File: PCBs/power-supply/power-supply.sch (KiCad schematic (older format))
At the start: 13 parts, among them U3 TL783

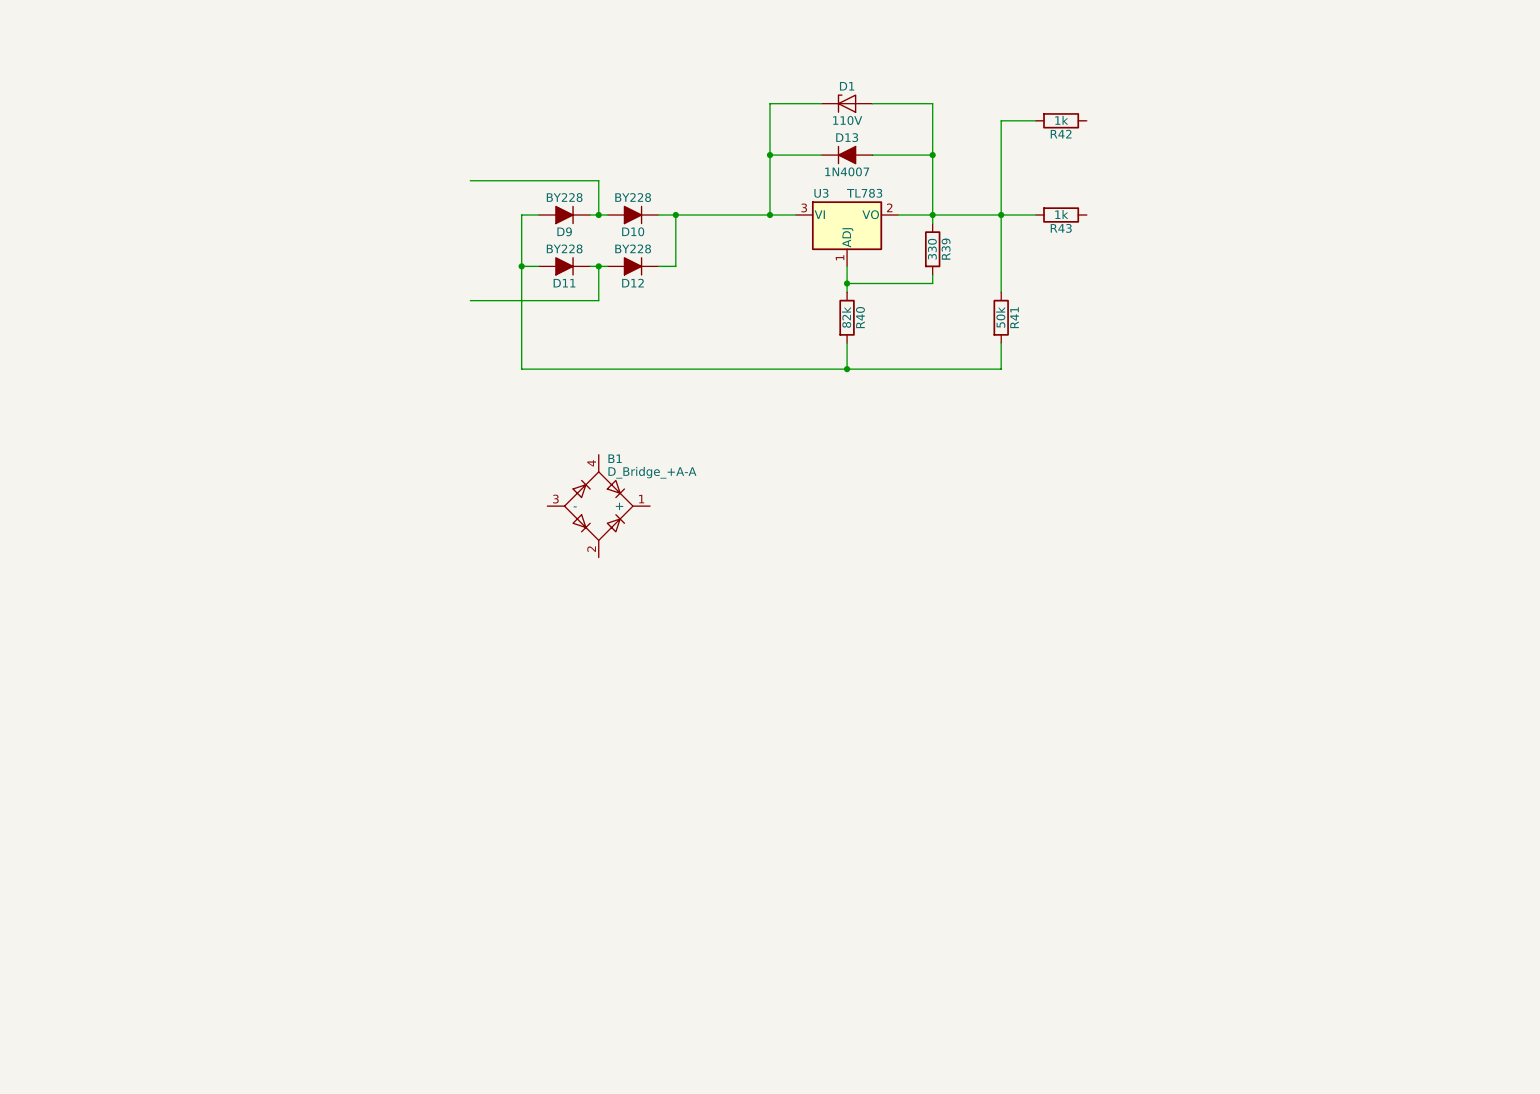
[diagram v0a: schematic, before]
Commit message: First kicad version of power supply .
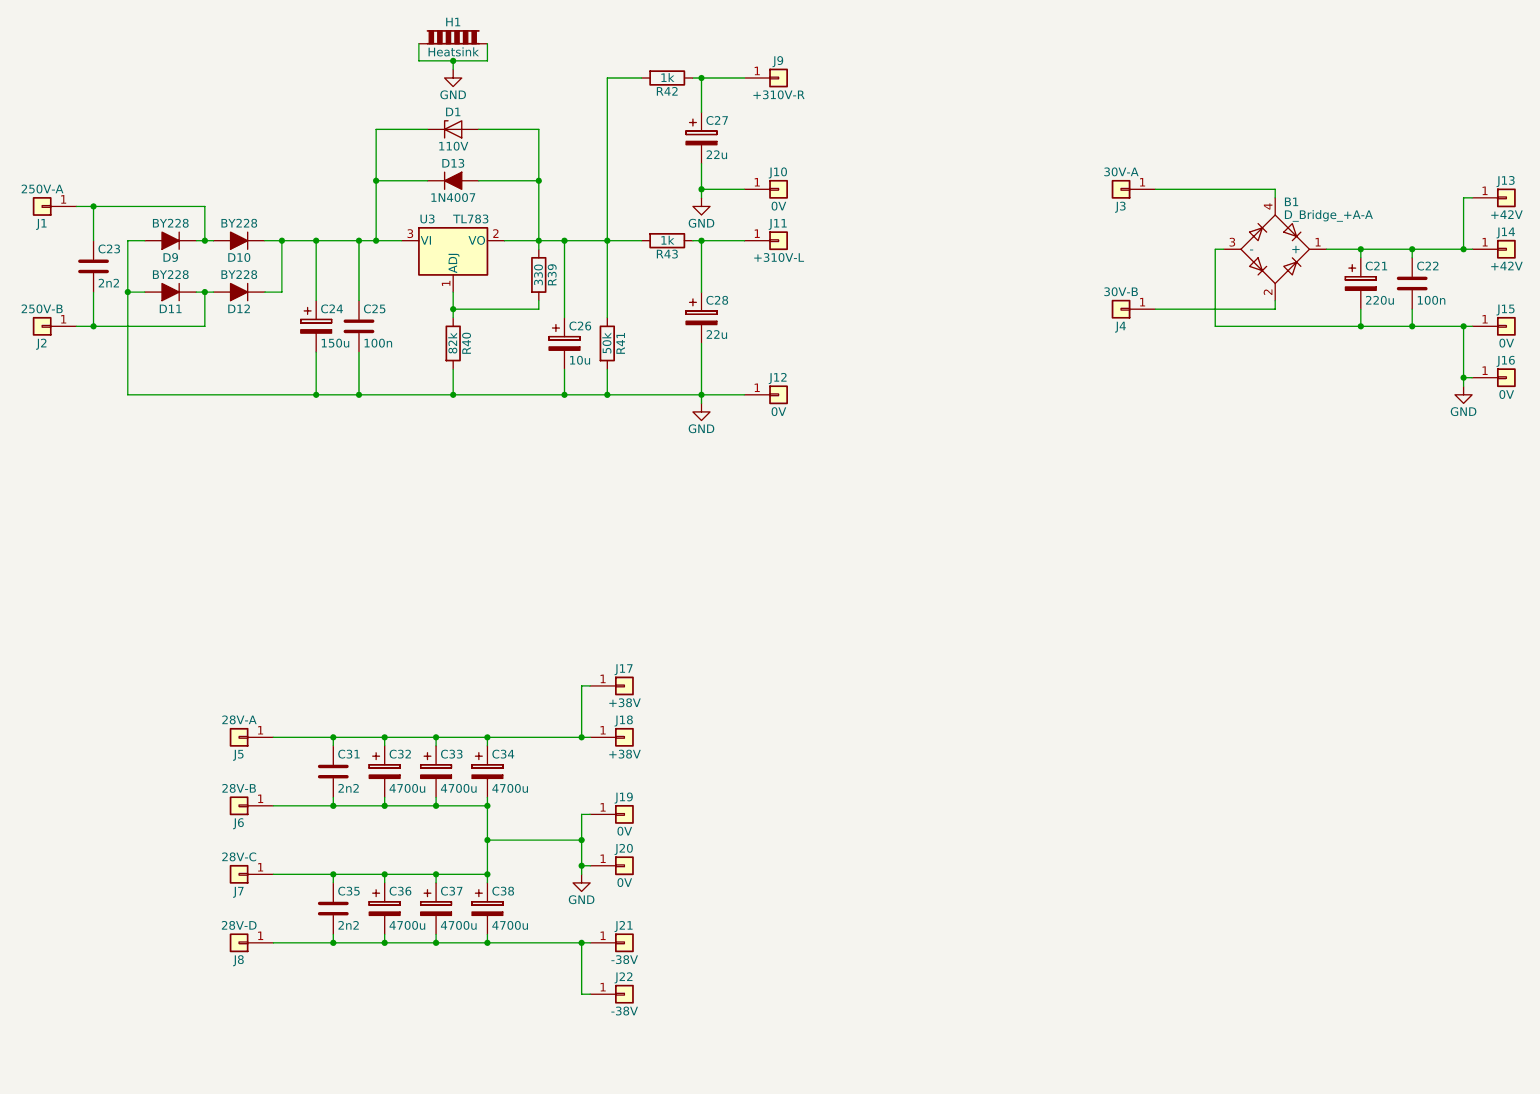
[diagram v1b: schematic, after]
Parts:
- added C21: 220u, Capacitors_THT:CP_Radial_D10.0mm_P3.80mm, symbol CP
- added C22: 100n, Capacitors_THT:C_Rect_L4.6mm_W2.0mm_P2.50mm_MKS02_FKP02, symbol C
- added C23: 2n2, Capacitors_THT:C_Rect_L28.0mm_W8.0mm_P22.50mm_MKS4, symbol C
- added C24: 150u, Capacitors_THT:CP_Radial_D7.5mm_P2.50mm, symbol CP
- added C25: 100n, Capacitors_THT:C_Rect_L18.0mm_W6.0mm_P15.00mm_FKS3_FKP3, symbol C
- added C26: 10u, Capacitors_THT:CP_Radial_D7.5mm_P2.50mm, symbol CP
- added C27, C28: 22u, Capacitors_THT:CP_Radial_D13.0mm_P5.00mm, symbol CP
- added C31, C35: 2n2, Capacitors_THT:C_Rect_L27.0mm_W9.0mm_P23.00mm, symbol C
- added C32, C33, C34, C36, C37, C38: 4700u, Capacitors_THT:CP_Radial_D35.0mm_P10.00mm_SnapIn, symbol CP
- added H1: Heatsink, Heatsinks:Heatsink_Fischer_SK104-STCB_35x13mm__2xDrill3.5mm_ScrewM3, symbol Peltier_Element
- added J1: 250V-A, Wire_Pads:SolderWirePad_single_2mmDrill, symbol Conn_01x01
- added J10, J12, J15, J16, J19, J20: 0V, Wire_Pads:SolderWirePad_single_2mmDrill, symbol Conn_01x01
- added J11: +310V-L, Wire_Pads:SolderWirePad_single_2mmDrill, symbol Conn_01x01
- added J13, J14: +42V, Wire_Pads:SolderWirePad_single_2mmDrill, symbol Conn_01x01
- added J17, J18: +38V, Wire_Pads:SolderWirePad_single_2mmDrill, symbol Conn_01x01
- added J2: 250V-B, Wire_Pads:SolderWirePad_single_2mmDrill, symbol Conn_01x01
- added J21, J22: -38V, Wire_Pads:SolderWirePad_single_2mmDrill, symbol Conn_01x01
- added J3: 30V-A, Wire_Pads:SolderWirePad_single_2mmDrill, symbol Conn_01x01
- added J4: 30V-B, Wire_Pads:SolderWirePad_single_2mmDrill, symbol Conn_01x01
- added J5: 28V-A, Wire_Pads:SolderWirePad_single_2mmDrill, symbol Conn_01x01
- added J6: 28V-B, Wire_Pads:SolderWirePad_single_2mmDrill, symbol Conn_01x01
- added J7: 28V-C, Wire_Pads:SolderWirePad_single_2mmDrill, symbol Conn_01x01
- added J8: 28V-D, Wire_Pads:SolderWirePad_single_2mmDrill, symbol Conn_01x01
- added J9: +310V-R, Wire_Pads:SolderWirePad_single_2mmDrill, symbol Conn_01x01
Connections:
- net labels added: GND
- wire segments 27 -> 89
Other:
- moved on the sheet: B1, D1, D10, D11, D12, D13, D9, R39, R40, R41, R42, R43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

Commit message: Small change.
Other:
- moved on the sheet: B1, C21, C22, C23, C24, C25, C26, C27, C28, C31, C32, C33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

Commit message: Changed footprints to kicad 5 names.
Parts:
- removed H1: Heatsink, Heatsinks:Heatsink_Fischer_SK104-STCB_35x13mm__2xDrill3.5mm_ScrewM3, symbol Peltier_Element
- added HS1: Heatsink_PAD, Heatsink:Heatsink_Fischer_SK104-STC-STIC_35x13mm_2xDrill2.5mm, symbol Mechanical:Heatsink_PAD
- B1: footprint Diodes_THT:Diode_Bridge_Round_D9.8mm -> Diode_THT:Diode_Bridge_Round_D9.8mm; symbol D_Bridge_+A-A -> power-supply-rescue:D_Bridge_+A-A
- C21: footprint Capacitors_THT:CP_Radial_D10.0mm_P3.80mm -> Capacitor_THT:CP_Radial_D10.0mm_P3.80mm; symbol CP -> power-supply-rescue:CP
- C22: footprint Capacitors_THT:C_Rect_L4.6mm_W2.0mm_P2.50mm_MKS02_FKP02 -> Capacitor_THT:C_Rect_L4.6mm_W2.0mm_P2.50mm_MKS02_FKP02; symbol C -> power-supply-rescue:C
- C23: footprint Capacitors_THT:C_Rect_L28.0mm_W8.0mm_P22.50mm_MKS4 -> Capacitor_THT:C_Rect_L28.0mm_W8.0mm_P22.50mm_MKS4; symbol C -> power-supply-rescue:C
- C24, C26: footprint Capacitors_THT:CP_Radial_D7.5mm_P2.50mm -> Capacitor_THT:CP_Radial_D7.5mm_P2.50mm; symbol CP -> power-supply-rescue:CP
- C25: footprint Capacitors_THT:C_Rect_L18.0mm_W6.0mm_P15.00mm_FKS3_FKP3 -> Capacitor_THT:C_Rect_L18.0mm_W6.0mm_P15.00mm_FKS3_FKP3; symbol C -> power-supply-rescue:C
- C27, C28: footprint Capacitors_THT:CP_Radial_D13.0mm_P5.00mm -> Capacitor_THT:CP_Radial_D13.0mm_P5.00mm; symbol CP -> power-supply-rescue:CP
- C31, C35: footprint Capacitors_THT:C_Rect_L27.0mm_W9.0mm_P23.00mm -> Capacitor_THT:C_Rect_L27.0mm_W9.0mm_P23.00mm; symbol C -> power-supply-rescue:C
- C32, C33, C34, C36, C37, C38: footprint Capacitors_THT:CP_Radial_D35.0mm_P10.00mm_SnapIn -> Capacitor_THT:CP_Radial_D35.0mm_P10.00mm_SnapIn; symbol CP -> power-supply-rescue:CP
- D1: footprint Diodes_THT:D_DO-15_P10.16mm_Horizontal -> Diode_THT:D_DO-15_P10.16mm_Horizontal; symbol D_Zener -> power-supply-rescue:D_Zener
- D10, D11, D12, D9: footprint Diodes_THT:D_T-1_P5.08mm_Horizontal -> Diode_THT:D_T-1_P5.08mm_Horizontal; symbol D_ALT -> power-supply-rescue:D_ALT
- D13: footprint Diodes_THT:D_DO-15_P10.16mm_Horizontal -> Diode_THT:D_DO-15_P10.16mm_Horizontal; symbol D_ALT -> power-supply-rescue:D_ALT
- J1, J10, J11, J12, J13, J14, J15, J16, J17, J18, J19, J2, J20, J21, J22, J3, J4, J5, J6, J7, J8, J9: footprint Wire_Pads:SolderWirePad_single_2mmDrill -> Connector_Wire:SolderWirePad_single_2mmDrill; symbol Conn_01x01 -> power-supply-rescue:Conn_01x01
- R39: footprint Resistors_THT:R_Axial_DIN0207_L6.3mm_D2.5mm_P10.16mm_Horizontal -> Resistor_THT:R_Axial_DIN0207_L6.3mm_D2.5mm_P10.16mm_Horizontal; symbol R -> power-supply-rescue:R
- R40, R41: footprint Resistors_THT:R_Axial_DIN0516_L15.5mm_D5.0mm_P20.32mm_Horizontal -> Resistor_THT:R_Axial_DIN0516_L15.5mm_D5.0mm_P20.32mm_Horizontal; symbol R -> power-supply-rescue:R
- R42, R43: footprint Resistors_THT:R_Axial_DIN0414_L11.9mm_D4.5mm_P15.24mm_Horizontal -> Resistor_THT:R_Axial_DIN0414_L11.9mm_D4.5mm_P15.24mm_Horizontal; symbol R -> power-supply-rescue:R
- U3: footprint TO_SOT_Packages_THT:TO-220_Vertical -> Package_TO_SOT_THT:TO-220-3_Vertical; symbol LM350_TO220 -> power-supply-rescue:LM350_TO220
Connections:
- net GND: now also HS1.1

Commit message: Fixed power-supply schematic.
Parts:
- B1: symbol power-supply-rescue:D_Bridge_+A-A -> Device:D_Bridge_+A-A
- C21, C24, C26, C27, C28, C32, C33, C34, C36, C37, C38: symbol power-supply-rescue:CP -> Device:CP
- C22, C23, C25, C31, C35: symbol power-supply-rescue:C -> Device:C
- D1: symbol power-supply-rescue:D_Zener -> Device:D_Zener
- D10, D11, D12, D13, D9: symbol power-supply-rescue:D_ALT -> Device:D_ALT
- J1, J10, J11, J12, J13, J14, J15, J16, J17, J18, J19, J2, J20, J21, J22, J3, J4, J5, J6, J7, J8, J9: symbol power-supply-rescue:Conn_01x01 -> Connector_Generic:Conn_01x01
- R39, R40, R41, R42, R43: symbol power-supply-rescue:R -> Device:R
- U3: symbol power-supply-rescue:LM350_TO220 -> Regulator_Linear:LM350_TO220
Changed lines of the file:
@@
 $EndDescr
 $Comp
-L power-supply-rescue:D_ALT D13
+L Device:D_ALT D13
 U 1 1 5ABAAB07
 P 3750 2100
@@
 $EndComp
 $Comp
-L power-supply-rescue:D_Zener D1
+L Device:D_Zener D1
 U 1 1 5ABAAC0E
 P 3750 1800
@@
 $EndComp
 $Comp
-L power-supply-rescue:D_Bridge_+A-A B1
+L Device:D_Bridge_+A-A B1
 U 1 1 5ABAAF42
 P 8200 2200
@@
 $EndComp
 $Comp
-L power-supply-rescue:D_ALT D10
+L Device:D_ALT D10
 U 1 1 5ABAB4F3
 P 2500 2450
@@
 $EndComp
 $Comp
-L power-supply-rescue:D_ALT D9
+L Device:D_ALT D9
 U 1 1 5ABAB5EE
 P 2100 2450
@@
 $EndComp
 $Comp
-L power-supply-rescue:D_ALT D11
+L Device:D_ALT D11
 U 1 1 5ABAB622
 P 2100 2750
@@
 $EndComp
 $Comp
-L power-supply-rescue:D_ALT D12
+L Device:D_ALT D12
 U 1 1 5ABAB653
 P 2500 2750
@@
 $EndComp
 $Comp
-L power-supply-rescue:R R40
+L Device:R R40
 U 1 1 5ABABD92
 P 3750 3050
@@
 $EndComp
 $Comp
-L power-supply-rescue:R R39
+L Device:R R39
 U 1 1 5ABABE2E
 P 4250 2650
@@
 $EndComp
 $Comp
-L power-supply-rescue:R R41
+L Device:R R41
 U 1 1 5ABABE96
 P 4650 3050
@@
 $EndComp
 $Comp
-L power-supply-rescue:R R43
+L Device:R R43
 U 1 1 5ABABED7
 P 5000 2450
@@
 $EndComp
 $Comp
-L power-supply-rescue:R R42
+L Device:R R42
 U 1 1 5ABABF35
 P 5000 1500
@@
 $EndComp
 $Comp
-L power-supply-rescue:LM350_TO220 U3
+L Regulator_Linear:LM350_TO220 U3
 U 1 1 5ABAD0FA
 P 3750 2450
@@
 $EndComp
 $Comp
-L power-supply-rescue:C C25
+L Device:C C25
 U 1 1 5ABBC641
 P 3200 2950
@@
 $EndComp
 $Comp
-L power-supply-rescue:C C23
+L Device:C C23
 U 1 1 5ABBCA16
 P 1650 2600
@@
 $EndComp
 $Comp
-L power-supply-rescue:C C31
+L Device:C C31
 U 1 1 5ABBCA5D
 P 2950 5300
@@
 $EndComp
 $Comp
-L power-supply-rescue:C C35
+L Device:C C35
 U 1 1 5ABBCAD3
 P 2950 6100
@@
 $EndComp
 $Comp
-L power-supply-rescue:C C22
+L Device:C C22
 U 1 1 5ABBCB32
 P 9000 2400
@@
 $EndComp
 $Comp
-L power-supply-rescue:CP C27
+L Device:CP C27
 U 1 1 5ABBCB78
 P 5200 1850
@@
 $EndComp
 $Comp
-L power-supply-rescue:CP C24
+L Device:CP C24
 U 1 1 5ABBCBF0
 P 2950 2950
@@
 $EndComp
 $Comp
-L power-supply-rescue:CP C28
+L Device:CP C28
 U 1 1 5ABBCC82
 P 5200 2900
@@
 $EndComp
 $Comp
-L power-supply-rescue:CP C26
+L Device:CP C26
 U 1 1 5ABBCCD7
 P 4400 3050
@@
 $EndComp
 $Comp
-L power-supply-rescue:CP C38
+L Device:CP C38
 U 1 1 5ABBCDBA
 P 3850 6100
@@
 $EndComp
 $Comp
-L power-supply-rescue:CP C37
+L Device:CP C37
 U 1 1 5ABBCE1E
 P 3550 6100
@@
 $EndComp
 $Comp
-L power-supply-rescue:CP C21
+L Device:CP C21
 U 1 1 5ABBCE87
 P 8700 2400
@@
 $EndComp
 $Comp
-L power-supply-rescue:CP C32
+L Device:CP C32
 U 1 1 5ABBCEF5
 P 3250 5300
@@
 $EndComp
 $Comp
-L power-supply-rescue:CP C33
+L Device:CP C33
 U 1 1 5ABBCF68
 P 3550 5300
@@
 $EndComp
 $Comp
-L power-supply-rescue:CP C34
+L Device:CP C34
 U 1 1 5ABBCFD2
 P 3850 5300
@@
 $EndComp
 $Comp
-L power-supply-rescue:CP C36
+L Device:CP C36
 U 1 1 5ABBD03F
 P 3250 6100
@@
 Connection ~ 3850 6300
 $Comp
-L power-supply-rescue:Conn_01x01 J10
+L Connector_Generic:Conn_01x01 J10
 U 1 1 5ABC81E4
 P 5650 2150
@@
 $EndComp
 $Comp
-L power-supply-rescue:Conn_01x01 J11
+L Connector_Generic:Conn_01x01 J11
 U 1 1 5ABC8263
 P 5650 2450
@@
 $EndComp
 $Comp
-L power-supply-rescue:Conn_01x01 J12
+L Connector_Generic:Conn_01x01 J12
 U 1 1 5ABC82D9
 P 5650 3350
@@
 $EndComp
 $Comp
-L power-supply-rescue:Conn_01x01 J14
+L Connector_Generic:Conn_01x01 J14
 U 1 1 5ABC836A
 P 9550 2200
@@
 $EndComp
 $Comp
-L power-supply-rescue:Conn_01x01 J15
+L Connector_Generic:Conn_01x01 J15
 U 1 1 5ABC8616
 P 9550 2650
@@
 $EndComp
 $Comp
-L power-supply-rescue:Conn_01x01 J18
+L Connector_Generic:Conn_01x01 J18
 U 1 1 5ABC86A5
 P 4650 5100
@@
 $EndComp
 $Comp
-L power-supply-rescue:Conn_01x01 J20
+L Connector_Generic:Conn_01x01 J20
 U 1 1 5ABC8749
 P 4650 5850
@@
 $EndComp
 $Comp
-L power-supply-rescue:Conn_01x01 J21
+L Connector_Generic:Conn_01x01 J21
 U 1 1 5ABC88C4
 P 4650 6300
@@
 $EndComp
 $Comp
-L power-supply-rescue:Conn_01x01 J8
+L Connector_Generic:Conn_01x01 J8
 U 1 1 5ABC895A
 P 2400 6300
@@
 $EndComp
 $Comp
-L power-supply-rescue:Conn_01x01 J7
+L Connector_Generic:Conn_01x01 J7
 U 1 1 5ABC8ADB
 P 2400 5900
@@
 $EndComp
 $Comp
-L power-supply-rescue:Conn_01x01 J6
+L Connector_Generic:Conn_01x01 J6
 U 1 1 5ABC8B71
 P 2400 5500
@@
 $EndComp
 $Comp
-L power-supply-rescue:Conn_01x01 J5
+L Connector_Generic:Conn_01x01 J5
 U 1 1 5ABC8DA2
 P 2400 5100
@@
 $EndComp
 $Comp
-L power-supply-rescue:Conn_01x01 J4
+L Connector_Generic:Conn_01x01 J4
 U 1 1 5ABC8EBA
 P 7300 2550
@@
 $EndComp
 $Comp
-L power-supply-rescue:Conn_01x01 J3
+L Connector_Generic:Conn_01x01 J3
 U 1 1 5ABC9217
 P 7300 1850
@@
 $EndComp
 $Comp
-L power-supply-rescue:Conn_01x01 J2
+L Connector_Generic:Conn_01x01 J2
 U 1 1 5ABC92C7
 P 1350 2950
@@
 $EndComp
 $Comp
-L power-supply-rescue:Conn_01x01 J1
+L Connector_Generic:Conn_01x01 J1
 U 1 1 5ABC937C
 P 1350 2250
@@
 $EndComp
 $Comp
-L power-supply-rescue:Conn_01x01 J9
+L Connector_Generic:Conn_01x01 J9
 U 1 1 5ABCA4E3
 P 5650 1500
@@
 $EndComp
 $Comp
-L power-supply-rescue:Conn_01x01 J13
+L Connector_Generic:Conn_01x01 J13
 U 1 1 5ABCC23B
 P 9550 1900
@@
 $EndComp
 $Comp
-L power-supply-rescue:Conn_01x01 J16
+L Connector_Generic:Conn_01x01 J16
 U 1 1 5ABCC2DF
 P 9550 2950
@@
 $EndComp
 $Comp
-L power-supply-rescue:Conn_01x01 J17
+L Connector_Generic:Conn_01x01 J17
 U 1 1 5ABCCF48
 P 4650 4800
@@
 $EndComp
 $Comp
-L power-supply-rescue:Conn_01x01 J19
+L Connector_Generic:Conn_01x01 J19
 U 1 1 5ABCCFF3
 P 4650 5550
@@
 $EndComp
 $Comp
-L power-supply-rescue:Conn_01x01 J22
+L Connector_Generic:Conn_01x01 J22
 U 1 1 5ABCD0A1
 P 4650 6600
